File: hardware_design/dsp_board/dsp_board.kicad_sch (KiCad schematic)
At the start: 25 parts, among them J1 USB4800-03-A_REVA, U1 TPD2S017DBVR, U2 AP2112K-3.3TRG1, U3 AP2112K-3.3TRG1, U4 24LC128-E/MS, U5 ESP32-S3-WROOM-1-N16R2

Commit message: Started PCB design
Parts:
- added C11, C14, C20, C24, C28: 10uF, Capacitor_Tantalum_SMD:CP_EIA-1608-08_AVX-J, symbol Device:C_Polarized
- added C12, C13, C15, C17, C18, C19, C23, C27: 100nF, Capacitor_SMD:C_0603_1608Metric, symbol Device:C_Small
- added C16, C29, C30: 47uF, Capacitor_Tantalum_SMD:CP_EIA-1608-08_AVX-J, symbol Device:C_Polarized
- added C21, C22: 22pF, Capacitor_SMD:C_0603_1608Metric, symbol Device:C_Small
- added C25: 3.3nF, Capacitor_SMD:C_0603_1608Metric, symbol Device:C_Small
- added C26: 56nF, Capacitor_SMD:C_0603_1608Metric, symbol Device:C_Small
- added C31, C32, C35, C36: 47uF, Capacitor_SMD:CP_Elec_5x4.5, symbol Device:C_Polarized
- added C33, C34, C37, C38: 5.6nF, Capacitor_Tantalum_SMD:CP_EIA-1608-08_AVX-J, symbol Device:C_Polarized
- added J2: SM06B-SRSS-TB(LF)(SN), JST_SM06B-SRSS-TB(LF)(SN), symbol SM06B-SRSS-TB_LF__SN_:SM06B-SRSS-TB(LF)(SN)
- added J3, J4, J5, J6, J7, J8: RCJ-041, CUI_RCJ-041, symbol RCJ-041:RCJ-041
- added Q2: BC807, Package_TO_SOT_SMD:SOT-23, symbol Transistor_BJT:BC807
- added R10: 100, Resistor_SMD:R_0603_1608Metric, symbol Device:R
- added R11: 475, Resistor_SMD:R_0603_1608Metric, symbol Device:R
- added R12, R13, R14: 18k, Resistor_SMD:R_0603_1608Metric, symbol Device:R
- added R15, R16, R17, R18: 560, Resistor_SMD:R_0603_1608Metric, symbol Device:R
- added R9: 1k, Resistor_SMD:R_0603_1608Metric, symbol Device:R
- added U6: ADAU1701JSTZ, QFP50P900X900X160-48N, symbol ADAU1701JSTZ:ADAU1701JSTZ
- added Y1: ECS-122.8-20-3X-EN-TR, XTAL_ECS-122.8-20-3X-EN-TR, symbol ECS-122.8-20-3X-EN-TR:ECS-122.8-20-3X-EN-TR
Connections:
- net +3.3V: now also C13.1, C14.1, C25.1, Q2.2 (E), R11.1, R9.1, U6.18 (IOVDD), U6.39 (PLL_MODE1)
- net +3.3VA: now also C17.1, C18.1, C19.1, C20.1, U6.34 (PVDD), U6.36 (AVDD), U6.48 (AVDD)
- net ADA_reset: now also U6.5 (~{RESET})
- net BOOT: now also J2.5; no longer R8.2
- net EN: now also R8.2, J2.4
- net I2C0_SCL: now also U6.23 (SCL/CCLK)
- net I2C0_SDA: now also U6.22 (SDA/COUT)
- net USB_DN: now also U5.13 (IO19)
- net USB_DP: now also U5.14 (IO20)
- net UART0_TX: now reaches U5.36 (RXD0)
- net UART0_TX: now also J2.3
- net UART0_RX: now reaches U5.37 (TXD0)
- net UART0_RX: now also J2.2
- net GND renamed GND1
- net GND1: now also C11.2, C12.1, C13.2, C14.2, C15.2, C16.2, C17.2, C18.2, C19.2, C20.2, C21.1, C22.1, C23.2, C24.2, C27.2, C28.2, C33.2, C34.2, C37.2, C38.2, J2.6, J3.1, J4.1, J5.1, J6.1, J7.1, J8.1, R14.2, U6.1 (AGND), U6.12 (DGND), U6.20 (ADDR1/CDATA/WB), U6.25 (DGND), U6.30 (RSVD), U6.33 (PGND), U6.37 (AGND), U6.38 (PLL_MODE0), U6.42 (AGND), U6.6 (SELFBOOT), U6.7 (ADDR0)
- new net: C32.2, R16.2
- new net: C21.2, R10.1, Y1.1
- new net: C26.1, R11.2
- new net: C34.1, J6.2, R16.1
- new net: C36.2, R18.2
- new net: C38.1, J8.2, R18.1
- new net: C15.1, C16.1, U6.40 (CM)
- new net: C37.1, J7.2, R17.1
- new net: Q2.1 (B), R9.2, U6.17 (VDRIVE)
- new net: C11.1, C12.2, Q2.3 (C), U6.13 (DVDD), U6.24 (DVDD)
- new net: C30.2, J4.2
- new net: C35.2, R17.2
- new net: C31.2, R15.2
- new net: J2.S1 (SHIELD), J2.S2 (SHIELD)
- new net: C33.1, J5.2, R15.1
- new net: C29.2, J3.2
- new net: C29.1, R12.2
- new net: C30.1, R13.2
- new net FILTA: C23.1, C24.1, U6.47 (FILTA)
- new net FILTD: C27.1, C28.1, U6.41 (FILTD)
- new net MCLKI: C22.2, U6.32 (MCLKI), Y1.2
- new net OSCO: R10.2, U6.31 (OSCO)
- new net PLL_LF: C25.2, C26.2, U6.35 (PLL_LF)
- new net adc1: R12.1, U6.2 (ADC0)
- new net adc2: R13.1, U6.4 (ADC1)
- new net adcRes: R14.1, U6.3 (ADC_RES)
- new net vout0: C31.1, U6.46 (VOUT0)
- new net vout1: C35.1, U6.45 (VOUT1)
- new net vout2: C32.1, U6.44 (VOUT2)
- new net vout3: C36.1, U6.43 (VOUT3)
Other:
- note added: "ADAU1701"
- note added: "Inputs"
- note added: "Interface"
- note added: "Outputs"
- moved on the sheet: C10, C9, R3, R4, R5, R6, R7, R8, U5

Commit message: PCB layout complete
PCB layout and routing complete.
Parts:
- removed R4, R5, R6: 2k20, Resistor_SMD:R_0603_1608Metric, symbol Device:R
- added D1: LED, Diode_SMD:D_0603_1608Metric, symbol Device:LED
- R3: value 2k20 -> 1k
- renumbered C8 to C1, C9 to C10, C10 to C11, C22 to C12, C23 to C13, C24 to C14, C11 to C15, C12 to C16, C25 to C17, C26 to C18, C15 to C19, C5 to C2, C27 to C20, C28 to C21, C16 to C22, C13 to C23, C14 to C24, C17 to C25, C18 to C26, C19 to C27, C20 to C28, C6 to C3, C31 to C30, C32 to C31, C33 to C32, C34 to C33, C30 to C34, C1 to C4, C2 to C5, C3 to C6, C4 to C7, C7 to C8, C21 to C9, J5 to J4, J6 to J5, J4 to J6, Q2 to Q1, R15 to R10, R16 to R11, R13 to R12, R17 to R13, R18 to R15, R10 to R3, R7 to R4, R8 to R5, R9 to R7, R11 to R8, R12 to R9, U6 to U5, U5 to U6
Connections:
- net +3.3V: no longer R3.1
- net ADA_reset: now also U6.20 (IO12); no longer U6.9 (IO16)
- net I2C0_SCL: now also U6.18 (IO10); no longer R3.2, U6.20 (IO12)
- net I2C0_SDA: now also U6.19 (IO11); no longer U6.21 (IO13)
- net I2C1_SCL: now also U6.30 (IO37); no longer U6.22 (IO14)
- net I2C1_SDA: now also U6.31 (IO38); no longer U6.8 (IO15)
- net at U6.4 (IO4): now also R3.1
- new net: D1.2 (A), R3.2
- new net GND: D1.1 (K)

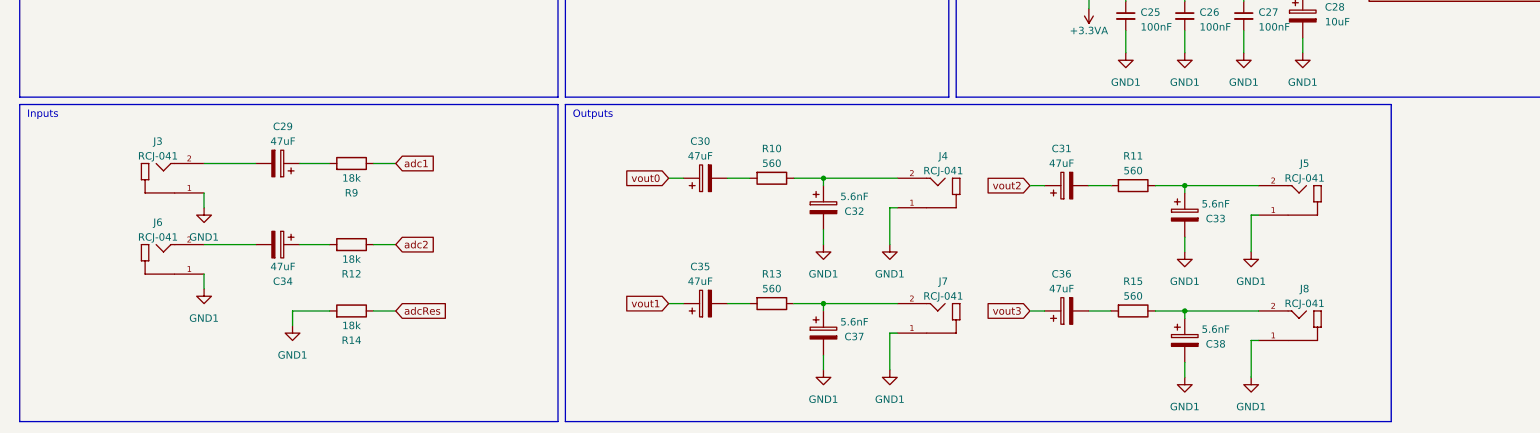
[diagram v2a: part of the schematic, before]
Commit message: Changed RCA connectors
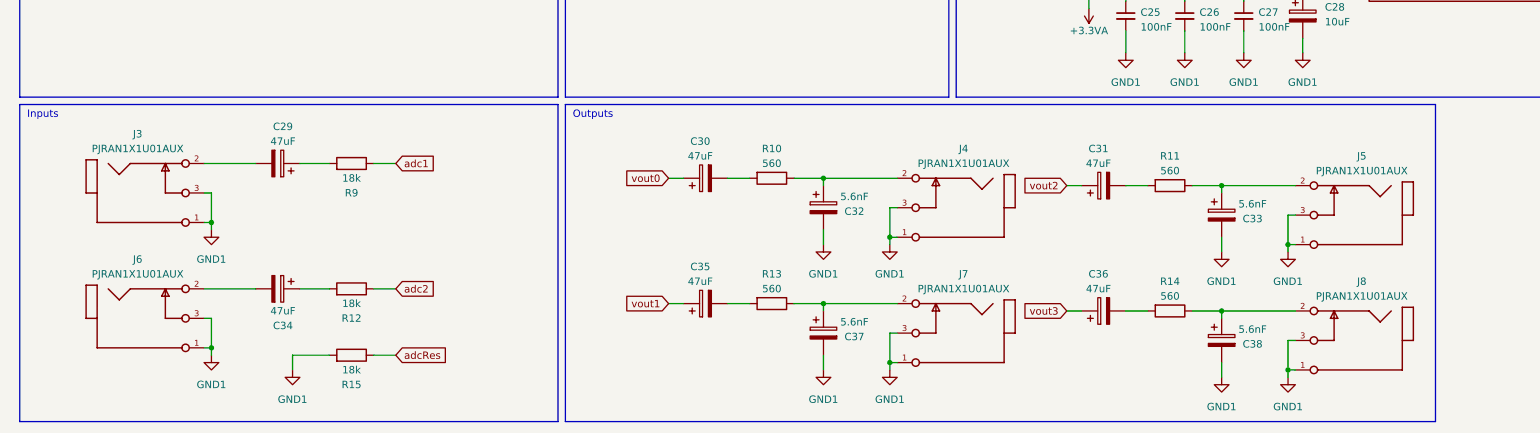
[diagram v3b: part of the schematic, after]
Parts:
- removed J3, J4, J5, J6, J7, J8: RCJ-041, CUI_RCJ-041, symbol RCJ-041:RCJ-041
- added J3, J4, J5, J6, J7, J8: PJRAN1X1U01AUX, PJRAN1X1U01AUX:PJRAN1X1U01X, symbol PJRAN1X1U01AUX:PJRAN1X1U01AUX
- renumbered R15 to R14, R14 to R15
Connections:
- net GND1: now also J3.1, J3.3, J4.1, J4.3, J5.1, J5.3, J6.1, J6.3, J7.1, J7.3, J8.1, J8.3
- net at C33.1, R11.1: now also J5.2
- net at C38.1, R14.1: now also J8.2
- net at C37.1, R13.1: now also J7.2
- net at C34.2: now also J6.2
- net at C32.1, R10.1: now also J4.2
- net at C29.2: now also J3.2
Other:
- moved on the sheet: C31, C33, C34, C36, C38, R11, R12, R14, R15

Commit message: documentation update
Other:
- company: (none) -> Perry Petiet
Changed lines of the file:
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@@
   (title_block
     (title "EasyDSP mainboard v0.1")
+    (company "Perry Petiet")
   )
   (junction (at 382.27 130.81) (diameter 0) (color 0 0 0 0)
